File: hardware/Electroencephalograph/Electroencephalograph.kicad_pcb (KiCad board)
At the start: 2 copper layers, 162 parts, among them J1 Conn_01x08_Male, U1 ADS1298IPAG, U10 TC1017-xCT, U11 TPS60403, U2 OPA330xxD, U3 TMS320LF2406PZ, U4 REF5025, U5 OPA350, U6 ADUM2401BRWZ, U7 THI3-0511, U8 TC1017-xCT, U9 TC1017-xCT, X1 2M048

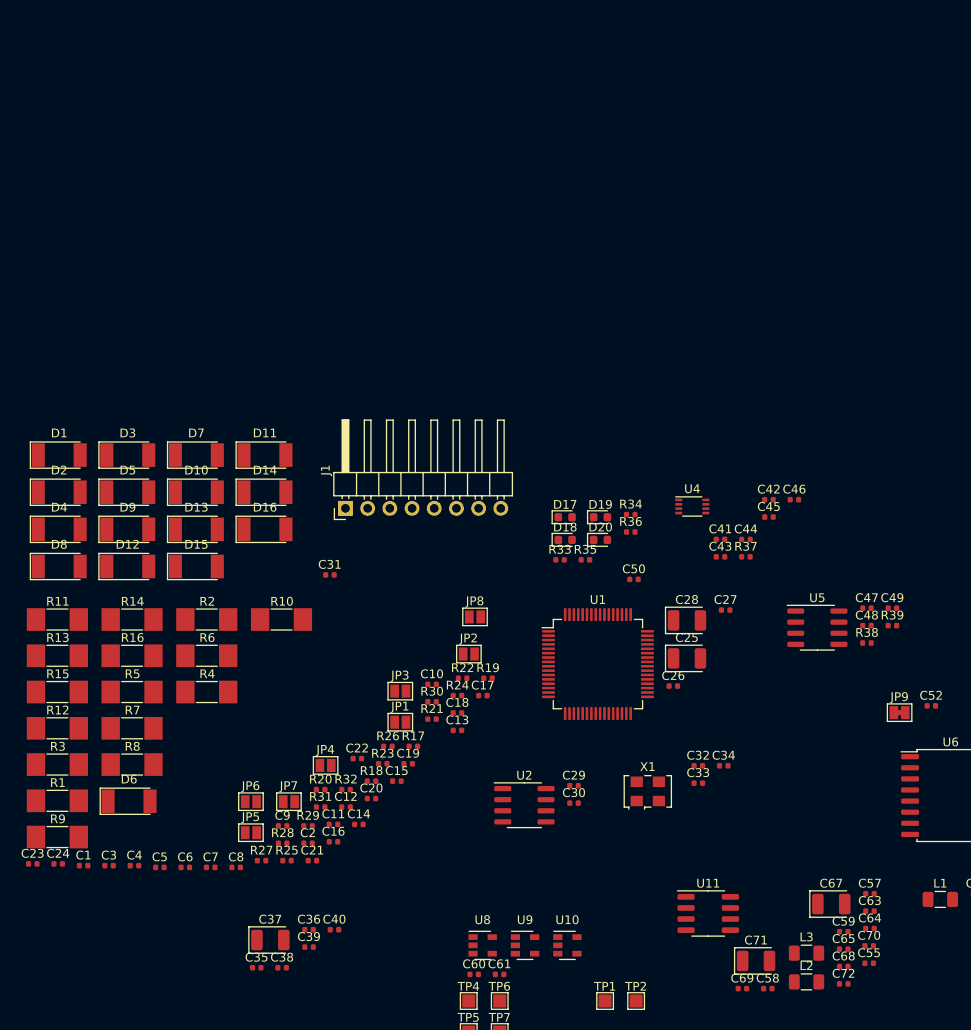
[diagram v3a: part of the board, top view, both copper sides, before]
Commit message: enqable separate electrodes for each point
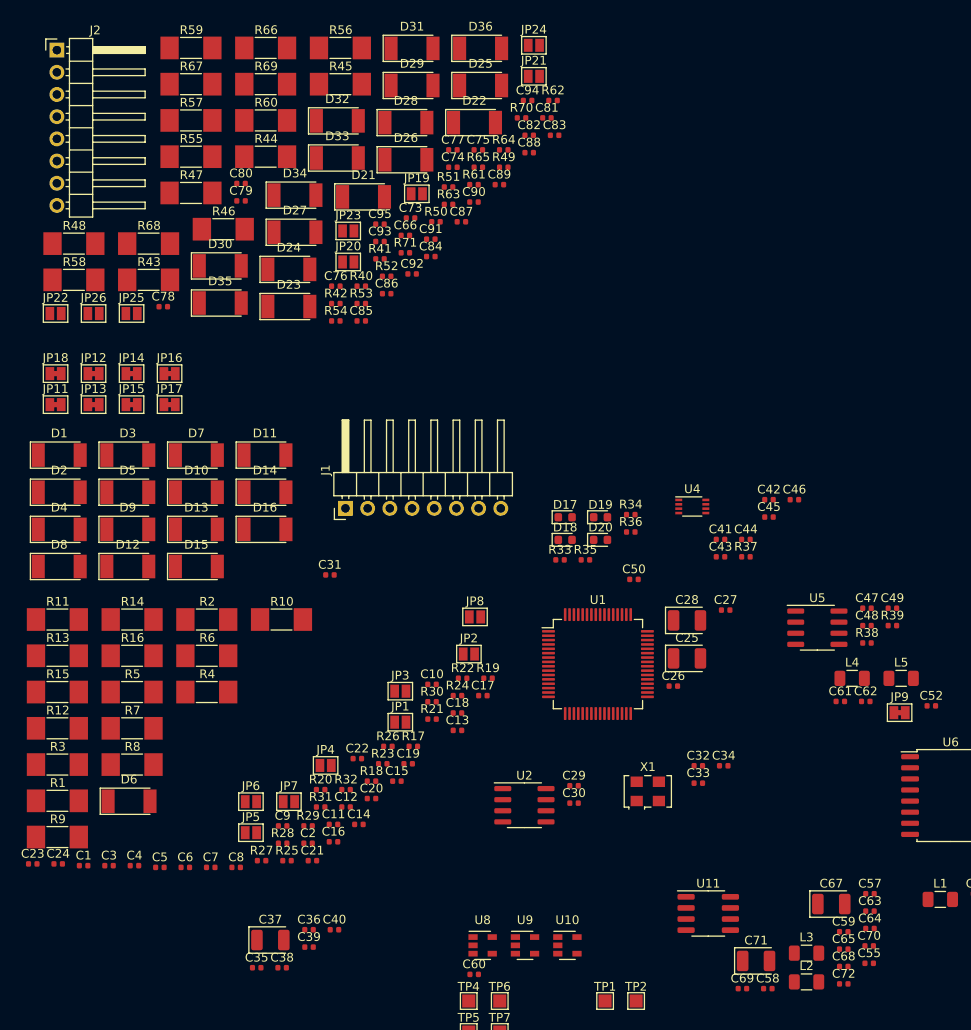
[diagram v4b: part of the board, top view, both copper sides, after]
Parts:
- added C62: 100n, Capacitor_SMD:C_0402_1005Metric, F.Cu at (225.2, 59.4)
- added C66: not mounted, Capacitor_SMD:C_0402_1005Metric, F.Cu at (172.5, 6.10)
- added C73: not mounted, Capacitor_SMD:C_0402_1005Metric, F.Cu at (173.1, 4.11)
- added C74: not mounted, Capacitor_SMD:C_0402_1005Metric, F.Cu at (177.9, -1.70)
- added C75: 47p, Capacitor_SMD:C_0402_1005Metric, F.Cu at (180.8, -3.69)
- added C76: 47p, Capacitor_SMD:C_0402_1005Metric, F.Cu at (164.5, 11.9)
- added C77: 47p, Capacitor_SMD:C_0402_1005Metric, F.Cu at (177.9, -3.69)
- added C78: 47p, Capacitor_SMD:C_0402_1005Metric, F.Cu at (144.8, 14.3)
- added C79: 47p, Capacitor_SMD:C_0402_1005Metric, F.Cu at (153.7, 2.15)
- added C80: 47p, Capacitor_SMD:C_0402_1005Metric, F.Cu at (153.7, 0.16)
- added C81: not mounted, Capacitor_SMD:C_0402_1005Metric, F.Cu at (188.7, -7.35)
- added C82: not mounted, Capacitor_SMD:C_0402_1005Metric, F.Cu at (186.6, -5.36)
- added C83: not mounted, Capacitor_SMD:C_0402_1005Metric, F.Cu at (189.5, -5.36)
- added C84: 47p, Capacitor_SMD:C_0402_1005Metric, F.Cu at (175.4, 8.52)
- added C85: 47p, Capacitor_SMD:C_0402_1005Metric, F.Cu at (167.4, 15.9)
- added C86: 47p, Capacitor_SMD:C_0402_1005Metric, F.Cu at (170.3, 12.8)
- added C87: 47p, Capacitor_SMD:C_0402_1005Metric, F.Cu at (178.9, 4.54)
- added C88: 47p, Capacitor_SMD:C_0402_1005Metric, F.Cu at (186.6, -3.37)
- added C89: 47p, Capacitor_SMD:C_0402_1005Metric, F.Cu at (183.2, 0.29)
- added C90: not mounted, Capacitor_SMD:C_0402_1005Metric, F.Cu at (180.3, 2.28)
- added C91: not mounted, Capacitor_SMD:C_0402_1005Metric, F.Cu at (175.4, 6.53)
- added C92: 47p, Capacitor_SMD:C_0402_1005Metric, F.Cu at (173.2, 10.5)
- added C93: 47p, Capacitor_SMD:C_0402_1005Metric, F.Cu at (169.6, 6.80)
- added C94: 47p, Capacitor_SMD:C_0402_1005Metric, F.Cu at (186.5, -9.34)
- added C95: 47p, Capacitor_SMD:C_0402_1005Metric, F.Cu at (169.6, 4.81)
- added D21: D, Diode_SMD:D_MELF, F.Cu at (167.7, 1.69)
- added D22: D, Diode_SMD:D_MELF, F.Cu at (180.4, -6.81)
- added D23: D, Diode_SMD:D_MELF, F.Cu at (159.1, 14.2)
- added D24: D, Diode_SMD:D_MELF, F.Cu at (159.1, 9.99)
- added D25: D, Diode_SMD:D_MELF, F.Cu at (181.1, -11.1)
- added D26: D, Diode_SMD:D_MELF, F.Cu at (172.5, -2.56)
- added D27: D, Diode_SMD:D_MELF, F.Cu at (159.8, 5.74)
- added D28: D, Diode_SMD:D_MELF, F.Cu at (172.5, -6.81)
- added D29: D, Diode_SMD:D_MELF, F.Cu at (173.2, -11.1)
- added D30: D, Diode_SMD:D_MELF, F.Cu at (151.3, 9.59)
- added D31: D, Diode_SMD:D_MELF, F.Cu at (173.2, -15.3)
- added D32: D, Diode_SMD:D_MELF, F.Cu at (164.7, -7.01)
- added D33: D, Diode_SMD:D_MELF, F.Cu at (164.7, -2.76)
- added D34: D, Diode_SMD:D_MELF, F.Cu at (159.8, 1.49)
- added D35: D, Diode_SMD:D_MELF, F.Cu at (151.3, 13.8)
- added D36: D, Diode_SMD:D_MELF, F.Cu at (181.1, -15.3)
- added J2: Conn_01x08_Male, Connector_PinHeader_2.54mm:PinHeader_1x08_P2.54mm_Horizontal, F.Cu at (132.6, -15.1)
- added JP11: NC, Jumper:SolderJumper-2_P1.3mm_Bridged_Pad1.0x1.5mm, F.Cu at (132.4, 25.5)
- added JP12: NC, Jumper:SolderJumper-2_P1.3mm_Bridged_Pad1.0x1.5mm, F.Cu at (136.8, 21.9)
- added JP13: NC, Jumper:SolderJumper-2_P1.3mm_Bridged_Pad1.0x1.5mm, F.Cu at (136.8, 25.5)
- added JP14: NC, Jumper:SolderJumper-2_P1.3mm_Bridged_Pad1.0x1.5mm, F.Cu at (141.1, 21.9)
- added JP15: NC, Jumper:SolderJumper-2_P1.3mm_Bridged_Pad1.0x1.5mm, F.Cu at (141.1, 25.5)
- added JP16: NC, Jumper:SolderJumper-2_P1.3mm_Bridged_Pad1.0x1.5mm, F.Cu at (145.5, 21.9)
- added JP17: NC, Jumper:SolderJumper-2_P1.3mm_Bridged_Pad1.0x1.5mm, F.Cu at (145.5, 25.5)
- added JP18: NC, Jumper:SolderJumper-2_P1.3mm_Bridged_Pad1.0x1.5mm, F.Cu at (132.4, 21.9)
- added JP19: Jumper_NO_Small, Jumper:SolderJumper-2_P1.3mm_Open_Pad1.0x1.5mm, F.Cu at (173.8, 1.34)
- added JP20: Jumper_NO_Small, Jumper:SolderJumper-2_P1.3mm_Open_Pad1.0x1.5mm, F.Cu at (165.9, 9.14)
- added JP21: Jumper_NO_Small, Jumper:SolderJumper-2_P1.3mm_Open_Pad1.0x1.5mm, F.Cu at (187.2, -12.1)
- added JP22: Jumper_NO_Small, Jumper:SolderJumper-2_P1.3mm_Open_Pad1.0x1.5mm, F.Cu at (132.4, 15.0)
- added JP23: Jumper_NO_Small, Jumper:SolderJumper-2_P1.3mm_Open_Pad1.0x1.5mm, F.Cu at (165.9, 5.59)
- added JP24: Jumper_NO_Small, Jumper:SolderJumper-2_P1.3mm_Open_Pad1.0x1.5mm, F.Cu at (187.2, -15.7)
- added JP25: Jumper_NO_Small, Jumper:SolderJumper-2_P1.3mm_Open_Pad1.0x1.5mm, F.Cu at (141.1, 15.0)
- added JP26: Jumper_NO_Small, Jumper:SolderJumper-2_P1.3mm_Open_Pad1.0x1.5mm, F.Cu at (136.8, 15.0)
- added L4: 3u3, Inductor_SMD:L_1206_3216Metric, F.Cu at (223.6, 56.8)
- added L5: 3u3, Inductor_SMD:L_1206_3216Metric, F.Cu at (229.2, 56.8)
- added R40: not mounted, Resistor_SMD:R_0402_1005Metric, F.Cu at (167.4, 11.9)
- added R41: not mounted, Resistor_SMD:R_0402_1005Metric, F.Cu at (169.6, 8.79)
- added R42: not mounted, Resistor_SMD:R_0402_1005Metric, F.Cu at (164.5, 13.9)
- added R43: 22k, Resistor_SMD:R_MELF_MMB-0207, F.Cu at (143.1, 11.2)
- added R44: 10k, Resistor_SMD:R_MELF_MMB-0207, F.Cu at (156.5, -2.91)
- added R45: 22k, Resistor_SMD:R_MELF_MMB-0207, F.Cu at (165.0, -11.2)
- added R46: 10k, Resistor_SMD:R_MELF_MMB-0207, F.Cu at (151.6, 5.39)
- added R47: 22k, Resistor_SMD:R_MELF_MMB-0207, F.Cu at (147.9, 1.24)
- added R48: 10k, Resistor_SMD:R_MELF_MMB-0207, F.Cu at (134.5, 7.04)
- added R49: not mounted, Resistor_SMD:R_0402_1005Metric, F.Cu at (183.7, -1.70)
- added R50: not mounted, Resistor_SMD:R_0402_1005Metric, F.Cu at (176.0, 4.54)
- added R51: not mounted, Resistor_SMD:R_0402_1005Metric, F.Cu at (177.4, 0.56)
- added R52: not mounted, Resistor_SMD:R_0402_1005Metric, F.Cu at (170.3, 10.8)
- added R53: not mounted, Resistor_SMD:R_0402_1005Metric, F.Cu at (167.4, 13.9)
- added R54: not mounted, Resistor_SMD:R_0402_1005Metric, F.Cu at (164.5, 15.9)
- added R55: 22k, Resistor_SMD:R_MELF_MMB-0207, F.Cu at (147.9, -2.91)
- added R56: 10k, Resistor_SMD:R_MELF_MMB-0207, F.Cu at (165.0, -15.4)
- added R57: 22k, Resistor_SMD:R_MELF_MMB-0207, F.Cu at (147.9, -7.06)
- added R58: 10k, Resistor_SMD:R_MELF_MMB-0207, F.Cu at (134.5, 11.2)
- added R59: 22k, Resistor_SMD:R_MELF_MMB-0207, F.Cu at (147.9, -15.4)
- added R60: 10k, Resistor_SMD:R_MELF_MMB-0207, F.Cu at (156.5, -7.06)
- added R61: not mounted, Resistor_SMD:R_0402_1005Metric, F.Cu at (180.3, 0.29)
- added R62: not mounted, Resistor_SMD:R_0402_1005Metric, F.Cu at (189.4, -9.34)
- added R63: not mounted, Resistor_SMD:R_0402_1005Metric, F.Cu at (177.4, 2.55)
- added R64: not mounted, Resistor_SMD:R_0402_1005Metric, F.Cu at (183.7, -3.69)
- added R65: not mounted, Resistor_SMD:R_0402_1005Metric, F.Cu at (180.8, -1.70)
- added R66: 22k, Resistor_SMD:R_MELF_MMB-0207, F.Cu at (156.5, -15.4)
- added R67: 10k, Resistor_SMD:R_MELF_MMB-0207, F.Cu at (147.9, -11.2)
- added R68: 22k, Resistor_SMD:R_MELF_MMB-0207, F.Cu at (143.1, 7.04)
- added R69: 10k, Resistor_SMD:R_MELF_MMB-0207, F.Cu at (156.5, -11.2)
- added R70: not mounted, Resistor_SMD:R_0402_1005Metric, F.Cu at (185.8, -7.35)
- added R71: not mounted, Resistor_SMD:R_0402_1005Metric, F.Cu at (172.5, 8.09)
- moved C61 50.0 mm to (222.2, 59.4)
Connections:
- net /EEGFrontend/ELECTRODE_1 renamed /EEGFrontendPositiveElectrode/ELECTRODE_1
- net /EEGFrontend/ELECTRODE_2 renamed /EEGFrontendPositiveElectrode/ELECTRODE_2
- net /EEGFrontend/ELECTRODE_3 renamed /EEGFrontendPositiveElectrode/ELECTRODE_3
- net /EEGFrontend/ELECTRODE_4 renamed /EEGFrontendPositiveElectrode/ELECTRODE_4
- net /EEGFrontend/ELECTRODE_5 renamed /EEGFrontendPositiveElectrode/ELECTRODE_5
- net /EEGFrontend/ELECTRODE_6 renamed /EEGFrontendPositiveElectrode/ELECTRODE_6
- net /EEGFrontend/ELECTRODE_7 renamed /EEGFrontendPositiveElectrode/ELECTRODE_7
- net /EEGFrontend/ELECTRODE_8 renamed /EEGFrontendPositiveElectrode/ELECTRODE_8
- net ECC_1 renamed ECC_1P
- net ECC_2 renamed ECC_2P
- net ECC_3 renamed ECC_3P
- net ECC_4 renamed ECC_4P
- net ECC_5 renamed ECC_5P
- net ECC_6 renamed ECC_6P
- net ECC_7 renamed ECC_7P
- net ECC_8 renamed ECC_8P
- C61 pad 1: VDDA -> Net-(C61-Pad1)
- C71 pad 1: Net-(C70-Pad1) -> Net-(C71-Pad1)
- C72 pad 1: Net-(C70-Pad1) -> Net-(C71-Pad1)
- TP6 pad 1: Net-(C70-Pad1) -> Net-(C71-Pad1)
- U1 pad 1: Net-(C31-Pad1) -> ECC_8N
- U1 pad 11: Net-(C31-Pad1) -> ECC_3N
- U1 pad 13: Net-(C31-Pad1) -> ECC_2N
- U1 pad 15: Net-(C31-Pad1) -> ECC_1N
- U1 pad 3: Net-(C31-Pad1) -> ECC_7N
- U1 pad 5: Net-(C31-Pad1) -> ECC_6N
- U1 pad 7: Net-(C31-Pad1) -> ECC_5N
- U1 pad 9: Net-(C31-Pad1) -> ECC_4N
- U10 pad 1: Net-(C70-Pad1) -> Net-(C71-Pad1)
- U10 pad 3: Net-(C70-Pad1) -> Net-(C71-Pad1)
- U8 pad 5: VDDA -> Net-(C61-Pad1)

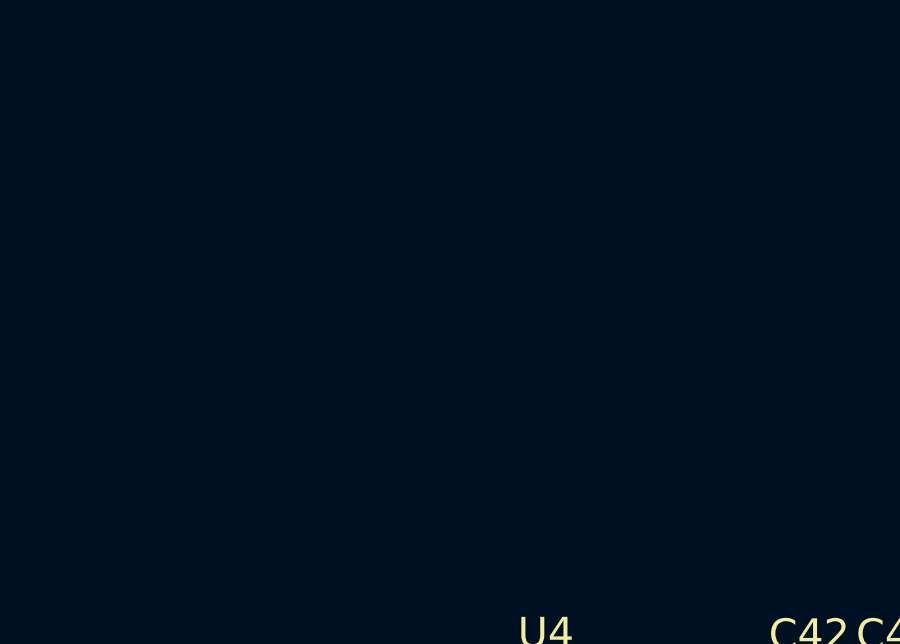
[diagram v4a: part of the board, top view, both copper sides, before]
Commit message: removed external clk and vref
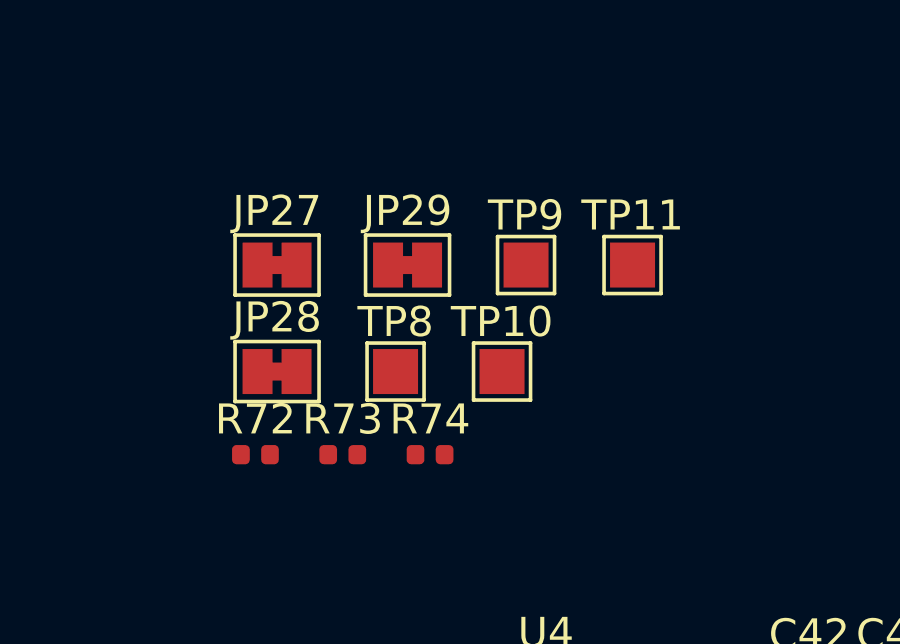
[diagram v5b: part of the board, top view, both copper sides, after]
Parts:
- added JP27: NC, Jumper:SolderJumper-2_P1.3mm_Bridged_Pad1.0x1.5mm, F.Cu at (196.3, 22.9)
- added JP28: NC, Jumper:SolderJumper-2_P1.3mm_Bridged_Pad1.0x1.5mm, F.Cu at (196.3, 26.4)
- added JP29: NC, Jumper:SolderJumper-2_P1.3mm_Bridged_Pad1.0x1.5mm, F.Cu at (200.7, 22.9)
- added R72: NC, Resistor_SMD:R_0402_1005Metric, F.Cu at (195.6, 29.2)
- added R73: NC, Resistor_SMD:R_0402_1005Metric, F.Cu at (198.5, 29.2)
- added R74: NC, Resistor_SMD:R_0402_1005Metric, F.Cu at (201.4, 29.2)
- added TP10: TestPoint, TestPoint:TestPoint_Pad_1.5x1.5mm, F.Cu at (203.8, 26.4)
- added TP11: TestPoint, TestPoint:TestPoint_Pad_1.5x1.5mm, F.Cu at (208.2, 22.9)
- added TP8: TestPoint, TestPoint:TestPoint_Pad_1.5x1.5mm, F.Cu at (200.3, 26.4)
- added TP9: TestPoint, TestPoint:TestPoint_Pad_1.5x1.5mm, F.Cu at (204.6, 22.9)
- C1, C2, C21, C22, C23, C24, C3, C4, C66, C73, C74, C81, C82, C83, C90, C91, R17, R18, R19, R20, R21, R22, R23, R24, R25, R26, R27, R28, R29, R30, R31, R32, R40, R41, R42, R49, R50, R51, R52, R53, R54, R61, R62, R63, R64, R65, R70, R71: value not mounted -> NC
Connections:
- U1 pad 32: (no net) -> VDDA
- U1 pad 34: (no net) -> EEG_MOSI
- U1 pad 35: (no net) -> Net-(JP28-Pad2)
- U1 pad 36: (no net) -> Net-(JP27-Pad2)
- U1 pad 38: (no net) -> Net-(JP29-Pad2)
- U1 pad 39: (no net) -> EEG_CS
- U1 pad 40: (no net) -> EEG_SCK
- U1 pad 43: (no net) -> EEG_MISO
- U6 pad 11: (no net) -> EEG_MISO
- U6 pad 12: (no net) -> EEG_CS
- U6 pad 13: (no net) -> EEG_MOSI
- U6 pad 14: (no net) -> EEG_SCK

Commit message: draft of PCB routing
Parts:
- removed C94, C95: 47p, Capacitor_SMD:C_0402_1005Metric
- removed R72, R73, R74: NC, Resistor_SMD:R_0402_1005Metric
- removed U10, U8, U9: TC1017-xCT, Package_TO_SOT_SMD:SOT-23-5
- removed U11: TPS60403, Package_SO:SOP-8_3.76x4.96mm_P1.27mm
- removed U7: THI3-0511, Relay_THT:Relay_DPDT_Omron_G6K-2P-Y
- removed X1: 2M048, Oscillator:Oscillator_SMD_EuroQuartz_XO53-4Pin_5.0x3.2mm
- added JP30: Jumper_NO_Small, Jumper:SolderJumper-2_P1.3mm_Open_Pad1.0x1.5mm, F.Cu at (79.4, 21.8)
- added JP31: Jumper_NO_Small, Jumper:SolderJumper-2_P1.3mm_Open_Pad1.0x1.5mm, F.Cu at (79.4, 37.1)
- added JP32: Jumper_NO_Small, Jumper:SolderJumper-2_P1.3mm_Open_Pad1.0x1.5mm, F.Cu at (79.4, 27.9)
- added L6: 22u, Inductor_SMD:L_7.3x7.3_H3.5, F.Cu at (120.9, 57.3)
- added TP12: TestPoint, TestPoint:TestPoint_Pad_1.5x1.5mm, F.Cu at (136.0, 55.3)
- added TP13: TestPoint, TestPoint:TestPoint_Pad_1.5x1.5mm, F.Cu at (137.9, 50.8)
- C1, C2, C21, C22, C3, C4, C73, C74, C81, C82, C83, C90, C91: value NC -> 47p
- C16, C17, C18, C7, C76, C77, C78, C8, C85, C86, C87, C9, C92, C93: value 47p -> NC
- C25: value 22u -> 1n; footprint Capacitor_Tantalum_SMD:CP_EIA-3528-21_Kemet-B -> Capacitor_SMD:C_0402_1005Metric
- C27, C35, C62: value 100n -> 2u2
- C28: footprint Capacitor_Tantalum_SMD:CP_EIA-3528-21_Kemet-B -> Capacitor_SMD:C_0402_1005Metric
- C29, C36, C56, C58, C59: value 100n -> 1u
- C31: value 1n -> 100n
- C32, C34, C40, C41, C69: value 1u -> 100n
- C38: value 100n -> 22u; footprint Capacitor_SMD:C_0402_1005Metric -> Capacitor_Tantalum_SMD:CP_EIA-3528-21_Kemet-B
- C45: value 10u -> 1u
- C46: value 100u -> 1u
- C48: value 22n -> 100n
- C49, C52: value 100n -> 220u; footprint Capacitor_SMD:C_0402_1005Metric -> Capacitor_SMD:CP_Elec_6.3x5.8
- C57: value 1u -> 100u; footprint Capacitor_SMD:C_0402_1005Metric -> Capacitor_SMD:CP_Elec_6.3x5.8
- C60: value 1u -> 100u; footprint Capacitor_SMD:C_0402_1005Metric -> Capacitor_Tantalum_SMD:CP_EIA-3528-21_Kemet-B
- C61, C63, C64, C65: value 1u -> 2u2
- C66: value NC -> 2u2
- C67: value 22u -> 100n; footprint Capacitor_Tantalum_SMD:CP_EIA-3528-21_Kemet-B -> Capacitor_SMD:C_0402_1005Metric
- C70, C72: value 1u -> 47p
- C71: value 22u -> 47p; footprint Capacitor_Tantalum_SMD:CP_EIA-3528-21_Kemet-B -> Capacitor_SMD:C_0402_1005Metric
- D1, D10, D11, D12, D13, D14, D15, D16, D2, D21, D22, D23, D24, D25, D26, D27, D28, D29, D3, D30, D31, D32, D33, D34, D35, D36, D4, D5, D6, D7, D8, D9, JP11, JP12, JP13, JP14, JP15, JP16: moved to B.Cu
- JP10, JP9: value Jumper_NC_Small -> NC; moved to B.Cu
- JP19, JP20, JP21, JP22: value Jumper_NO_Small -> NC; footprint Jumper:SolderJumper-2_P1.3mm_Open_Pad1.0x1.5mm -> Jumper:SolderJumper-2_P1.3mm_Bridged_Pad1.0x1.5mm
- JP23, JP24: value Jumper_NO_Small -> Jumper_NC_Small; footprint Jumper:SolderJumper-2_P1.3mm_Open_Pad1.0x1.5mm -> Jumper:SolderJumper-2_P1.3mm_Bridged_Pad1.0x1.5mm
- JP27, JP28, JP29: value NC -> Jumper_NO_Small; footprint Jumper:SolderJumper-2_P1.3mm_Bridged_Pad1.0x1.5mm -> Jumper:SolderJumper-2_P1.3mm_Open_Pad1.0x1.5mm
- L1, L2, L3, L4, L5: value 3u3 -> 22u; footprint Inductor_SMD:L_1206_3216Metric -> Inductor_SMD:L_7.3x7.3_H3.5
- R10, R12, R46, R48, R58, R60, R69, R8: value 10k -> NC; footprint Resistor_SMD:R_MELF_MMB-0207 -> Resistor_SMD:R_0402_1005Metric
- R11, R47, R59, R68, R7, R9: value 22k -> NC; footprint Resistor_SMD:R_MELF_MMB-0207 -> Resistor_SMD:R_0402_1005Metric
- R14, R2: value 10k -> 22k
- R17, R18, R27, R28: value NC -> 10k; footprint Resistor_SMD:R_0402_1005Metric -> Resistor_SMD:R_MELF_MMB-0207
- R25, R26, R40, R41, R42, R52, R53, R54, R64, R65: value NC -> 22k; footprint Resistor_SMD:R_0402_1005Metric -> Resistor_SMD:R_MELF_MMB-0207
- R37: value 100R -> NC
- R38: value 10R -> NC
- R39: value 100k -> NC
- R43, R45, R5, R55, R57, R66: value 22k -> 10k
- U4: value REF5025 -> THI3-0511; footprint Package_SO:VSSOP-8_2.3x2mm_P0.5mm -> Relay_THT:Relay_DPDT_Omron_G6K-2P-Y
- U5: value OPA350 -> ADUM2401BRWZ; footprint Package_SO:SOIC-8_3.9x4.9mm_P1.27mm -> Package_SO:SOIC-16W_7.5x10.3mm_P1.27mm
- U6: value ADUM2401BRWZ -> TPS60403; footprint Package_SO:SOIC-16W_7.5x10.3mm_P1.27mm -> Package_SO:SOP-8_3.76x4.96mm_P1.27mm
- moved U3 186.8 mm to (88.9, 93.5)
- moved C72 169.2 mm to (67.1, 25.4), turned to 90 degrees
- moved C70 166.9 mm to (67.1, 35.0), turned to 90 degrees
- moved JP10 159.0 mm to (84.8, 58.9), turned to 180 degrees
- moved C71 152.5 mm to (67.1, 43.7), turned to 90 degrees
- moved JP9 144.3 mm to (84.8, 65.0), turned to 180 degrees
- moved C47 137.2 mm to (89.4, 29.5)
- moved L1 137.1 mm to (106.7, 30.5), turned to 90 degrees
- moved L2 134.0 mm to (99.1, 30.5), turned to 90 degrees
- moved C48 133.1 mm to (94.0, 29.5)
- moved C81 127.7 mm to (67.1, 31.5), turned to 90 degrees
- moved R64 125.8 mm to (62.1, 28.4), turned to 180 degrees
- moved R65 125.1 mm to (62.1, 37.6), turned to 180 degrees
- moved C88 123.8 mm to (67.0, 28.4), turned to 90 degrees
- moved R39 122.6 mm to (105.6, 48.8), turned to 180 degrees
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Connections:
- C1 pad 1: ECC_1P -> Net-(C1-Pad1)
- C1 pad 2: Net-(C1-Pad2) -> GNDA
- C16 pad 1: Net-(C16-Pad1) -> ECC_1N
- C16 pad 2: GNDA -> Net-(C13-Pad1)
- C17 pad 1: Net-(C17-Pad1) -> ECC_3P
- C17 pad 2: GNDA -> Net-(C15-Pad1)
- C18 pad 1: Net-(C18-Pad1) -> ECC_4N
- C18 pad 2: GNDA -> Net-(C14-Pad1)
- C2 pad 1: ECC_2P -> Net-(C2-Pad1)
- C2 pad 2: Net-(C2-Pad2) -> GNDA
- C21 pad 1: ECC_6P -> Net-(C21-Pad1)
- C21 pad 2: Net-(C16-Pad1) -> GNDA
- C22 pad 1: ECC_5P -> Net-(C22-Pad1)
- C22 pad 2: Net-(C14-Pad1) -> GNDA
- C23 pad 1: ECC_8P -> ECC_2P
- C23 pad 2: Net-(C20-Pad1) -> Net-(C22-Pad1)
- C24 pad 1: ECC_7P -> ECC_3N
- C24 pad 2: Net-(C18-Pad1) -> Net-(C21-Pad1)
- C26 pad 1: Net-(C26-Pad1) -> VDDA
- C26 pad 2: VDDA -> GNDA
- C28 pad 1: VDDA -> Net-(C28-Pad1)
- C29 pad 1: VDDA -> GNDA
- C29 pad 2: GNDA -> VDDA
- C3 pad 1: ECC_4P -> Net-(C3-Pad1)
- C3 pad 2: Net-(C12-Pad1) -> GNDA
- C30 pad 1: VDDA -> GNDA
- C30 pad 2: GNDA -> VDDA
- C31 pad 1: Net-(C31-Pad1) -> Net-(C28-Pad1)
- C31 pad 2: VDDA -> GNDA
- C32 pad 1: Net-(C26-Pad1) -> GNDA
- C33 pad 1: Net-(C33-Pad1) -> GNDA
- C34 pad 1: Net-(C34-Pad1) -> VDDA
- C34 pad 2: VDDA -> GNDA
- C35 pad 2: VDDA -> GNDA
- C36 pad 1: VDDA -> Net-(C36-Pad1)
- C36 pad 2: VDDA -> GNDA
- C37 pad 1: /EEGAcquisition/V_REF -> Net-(C37-Pad1)
- C37 pad 2: VDDA -> GNDA
- C38 pad 1: /EEGAcquisition/V_REF -> Net-(C38-Pad1)
- C38 pad 2: VDDA -> GNDA
- C39 pad 1: VDDA -> Net-(C39-Pad1)
- C39 pad 2: VDDA -> GNDA
- C4 pad 1: ECC_3P -> Net-(C4-Pad1)
- C4 pad 2: Net-(C10-Pad1) -> GNDA
- C40 pad 1: VDDA -> Net-(C37-Pad1)
- C40 pad 2: VDDA -> GNDA
- C41 pad 1: VDDA -> GNDA
- C41 pad 2: VDDA -> Net-(C41-Pad2)
- C42 pad 1: VDDA -> Net-(C42-Pad1)
- C42 pad 2: VDDA -> GNDA
- C43 pad 2: VDDA -> GNDA
- C44 pad 1: Net-(C44-Pad1) -> GNDA
- C45 pad 1: Net-(C45-Pad1) -> VDDA
- C45 pad 2: VDDA -> GNDA
- C46 pad 1: Net-(C46-Pad1) -> VDDA
- C46 pad 2: VDDA -> GNDA
- C47 pad 1: GNDA -> VDDA
- C47 pad 2: VDDA -> GNDA
- C48 pad 1: Net-(C48-Pad1) -> VDDA
- C48 pad 2: Net-(C48-Pad2) -> GNDA
- C49 pad 1: GNDA -> VDDA
- C49 pad 2: VDDA -> GNDA
- C50 pad 1: VDDA -> Net-(C50-Pad1)
- C52 pad 1: VDDA -> Net-(C52-Pad1)
- C53 pad 1: ECC_POWER_SUPPLY -> Net-(C52-Pad1)
- C55 pad 1: VDDA -> ECC_POWER_SUPPLY
- C56 pad 1: Net-(C56-Pad1) -> ECC_POWER_SUPPLY
- C57 pad 1: VDDA -> Net-(C57-Pad1)
- C57 pad 2: VDDA -> GNDA
- C58 pad 1: VDDA -> (no net)
- C58 pad 2: VDDA -> Net-(C58-Pad2)
- C59 pad 1: VDDA -> Net-(C59-Pad1)
- C6 pad 1: Net-(C1-Pad2) -> Net-(C6-Pad1)
- C60 pad 1: ECC_POWER_SUPPLY -> Net-(C60-Pad1)
- C61 pad 1: Net-(C61-Pad1) -> ECC_POWER_SUPPLY
- C62 pad 1: VDDA -> ECC_POWER_SUPPLY
- C63 pad 1: Net-(C63-Pad1) -> Net-(C60-Pad1)
- C64 pad 1: ECC_POWER_SUPPLY -> VDDA
- C65 pad 1: (no net) -> VDDA
- C65 pad 2: Net-(C65-Pad2) -> GNDA
- C66 pad 1: ECC_1N -> VDDA
- C66 pad 2: Net-(C66-Pad2) -> GNDA
- C67 pad 1: ECC_POWER_SUPPLY -> VDDA
- C68 pad 1: ECC_POWER_SUPPLY -> VDDA
- C68 pad 2: GNDA -> VDDA
- C69 pad 1: Net-(C69-Pad1) -> VDDA
- C69 pad 2: GNDA -> VDDA
- C7 pad 1: Net-(C7-Pad1) -> ECC_1P
- C7 pad 2: GNDA -> Net-(C5-Pad1)
- C72 pad 1: Net-(C71-Pad1) -> Net-(C72-Pad1)
- C73 pad 1: ECC_2N -> Net-(C73-Pad1)
- C73 pad 2: Net-(C73-Pad2) -> GNDA
- C74 pad 1: ECC_3N -> Net-(C74-Pad1)
- C74 pad 2: Net-(C74-Pad2) -> GNDA
- C76 pad 1: Net-(C66-Pad2) -> ECC_5P
- C76 pad 2: GNDA -> Net-(C74-Pad1)
- C77 pad 1: Net-(C77-Pad1) -> ECC_6N
- C77 pad 2: GNDA -> Net-(C73-Pad1)
- C78 pad 1: Net-(C73-Pad2) -> ECC_8P
- C78 pad 2: GNDA -> Net-(C75-Pad1)
- C8 pad 1: Net-(C2-Pad2) -> ECC_2N
- C8 pad 2: GNDA -> Net-(C4-Pad1)
- C80 pad 1: Net-(C74-Pad2) -> Net-(C80-Pad1)
- C81 pad 1: ECC_6N -> Net-(C81-Pad1)
- C81 pad 2: Net-(C81-Pad2) -> GNDA
- C82 pad 1: ECC_4N -> Net-(C82-Pad1)
- C82 pad 2: Net-(C82-Pad2) -> GNDA
- C83 pad 1: ECC_5N -> Net-(C83-Pad1)
- C83 pad 2: Net-(C83-Pad2) -> GNDA
- C85 pad 1: Net-(C81-Pad2) -> ECC_5N
- C85 pad 2: GNDA -> Net-(C82-Pad1)
- C86 pad 1: Net-(C86-Pad1) -> ECC_7P
- C86 pad 2: GNDA -> Net-(C84-Pad1)
- C87 pad 1: Net-(C82-Pad2) -> ECC_8N
- C87 pad 2: GNDA -> Net-(C83-Pad1)
- C89 pad 1: Net-(C83-Pad2) -> Net-(C89-Pad1)
- C9 pad 1: Net-(C9-Pad1) -> ECC_4P
- C9 pad 2: GNDA -> Net-(C6-Pad1)
- C90 pad 1: ECC_8N -> Net-(C90-Pad1)
- C90 pad 2: Net-(C90-Pad2) -> GNDA
- C91 pad 1: ECC_7N -> Net-(C91-Pad1)
- C91 pad 2: Net-(C91-Pad2) -> GNDA
- C92 pad 1: Net-(C92-Pad1) -> ECC_6P
- C92 pad 2: GNDA -> Net-(C91-Pad1)
- C93 pad 1: Net-(C90-Pad2) -> ECC_7N
- C93 pad 2: GNDA -> Net-(C90-Pad1)
- D1 pad 2: Net-(C1-Pad2) -> Net-(C5-Pad1)
- D10 pad 1: VDDA -> Net-(C15-Pad1)
- D10 pad 2: Net-(C14-Pad1) -> VDDA
- D11 pad 1: Net-(C16-Pad1) -> VDDA
- D11 pad 2: VDDA -> Net-(C14-Pad1)
- D13 pad 2: Net-(C20-Pad1) -> Net-(C22-Pad1)
- D14 pad 1: VDDA -> Net-(C22-Pad1)
- D14 pad 2: Net-(D14-Pad2) -> VDDA
- D15 pad 1: Net-(C20-Pad1) -> VDDA
- D15 pad 2: VDDA -> Net-(C21-Pad1)
- D16 pad 1: Net-(D14-Pad2) -> Net-(C21-Pad1)
- D2 pad 1: VDDA -> Net-(C5-Pad1)
- D2 pad 2: Net-(C2-Pad2) -> VDDA
- D21 pad 2: Net-(C66-Pad2) -> Net-(C74-Pad1)
- D22 pad 1: VDDA -> Net-(C74-Pad1)
- D22 pad 2: Net-(C73-Pad2) -> VDDA
- D23 pad 2: Net-(C74-Pad2) -> Net-(C73-Pad1)
- D24 pad 1: Net-(C74-Pad2) -> Net-(C73-Pad1)
- D25 pad 1: Net-(C66-Pad2) -> VDDA
- D25 pad 2: VDDA -> Net-(C75-Pad1)
- D26 pad 1: Net-(C73-Pad2) -> Net-(C75-Pad1)
- D27 pad 2: Net-(C81-Pad2) -> Net-(C82-Pad1)
- D28 pad 1: VDDA -> Net-(C82-Pad1)
- D28 pad 2: Net-(C82-Pad2) -> VDDA
- D29 pad 2: Net-(C83-Pad2) -> Net-(C84-Pad1)
- D3 pad 1: Net-(C1-Pad2) -> VDDA
- D3 pad 2: VDDA -> Net-(C4-Pad1)
- D30 pad 1: Net-(C81-Pad2) -> Net-(C84-Pad1)
- D31 pad 1: Net-(C82-Pad2) -> VDDA
- D31 pad 2: VDDA -> Net-(C83-Pad1)
- D32 pad 1: Net-(C83-Pad2) -> Net-(C83-Pad1)
- D33 pad 2: Net-(C90-Pad2) -> Net-(C91-Pad1)
- D34 pad 1: VDDA -> Net-(C91-Pad1)
- D34 pad 2: Net-(D34-Pad2) -> VDDA
- D35 pad 1: Net-(C90-Pad2) -> VDDA
- D35 pad 2: VDDA -> Net-(C90-Pad1)
- D36 pad 1: Net-(D34-Pad2) -> Net-(C90-Pad1)
- D4 pad 1: Net-(C2-Pad2) -> Net-(C4-Pad1)
- D5 pad 2: Net-(C12-Pad1) -> Net-(C6-Pad1)
- D6 pad 1: VDDA -> Net-(C6-Pad1)
- D6 pad 2: Net-(C10-Pad1) -> VDDA
- D7 pad 1: Net-(C10-Pad1) -> VDDA
- D7 pad 2: VDDA -> Net-(C13-Pad1)
- D8 pad 1: Net-(C12-Pad1) -> Net-(C13-Pad1)
- D9 pad 2: Net-(C16-Pad1) -> Net-(C15-Pad1)
- J1 pad 1: /EEGFrontendPositiveElectrode/ELECTRODE_1 -> /EEGFrontendElectrode1To4/ELECTRODE_1
- J1 pad 2: /EEGFrontendPositiveElectrode/ELECTRODE_2 -> /EEGFrontendElectrode1To4/ELECTRODE_2
- J1 pad 3: /EEGFrontendPositiveElectrode/ELECTRODE_3 -> /EEGFrontendElectrode1To4/ELECTRODE_3
- J1 pad 4: /EEGFrontendPositiveElectrode/ELECTRODE_4 -> /EEGFrontendElectrode1To4/ELECTRODE_4
- J1 pad 5: /EEGFrontendPositiveElectrode/ELECTRODE_5 -> /EEGFrontendElectrode1To4/ELECTRODE_5
- J1 pad 6: /EEGFrontendPositiveElectrode/ELECTRODE_6 -> /EEGFrontendElectrode1To4/ELECTRODE_6
- J1 pad 7: /EEGFrontendPositiveElectrode/ELECTRODE_7 -> /EEGFrontendElectrode1To4/ELECTRODE_7
- J1 pad 8: /EEGFrontendPositiveElectrode/ELECTRODE_8 -> /EEGFrontendElectrode1To4/ELECTRODE_8
- J2 pad 1: /EEGFrontendNegativeElectrode/ELECTRODE_1 -> /EEGFrontendElectrode5To8/ELECTRODE_1
- J2 pad 2: /EEGFrontendNegativeElectrode/ELECTRODE_2 -> /EEGFrontendElectrode5To8/ELECTRODE_2
- J2 pad 3: /EEGFrontendNegativeElectrode/ELECTRODE_3 -> /EEGFrontendElectrode5To8/ELECTRODE_3
- J2 pad 4: /EEGFrontendNegativeElectrode/ELECTRODE_4 -> /EEGFrontendElectrode5To8/ELECTRODE_4
- J2 pad 5: /EEGFrontendNegativeElectrode/ELECTRODE_5 -> /EEGFrontendElectrode5To8/ELECTRODE_5
- J2 pad 6: /EEGFrontendNegativeElectrode/ELECTRODE_6 -> /EEGFrontendElectrode5To8/ELECTRODE_6
- J2 pad 7: /EEGFrontendNegativeElectrode/ELECTRODE_7 -> /EEGFrontendElectrode5To8/ELECTRODE_7
- J2 pad 8: /EEGFrontendNegativeElectrode/ELECTRODE_8 -> /EEGFrontendElectrode5To8/ELECTRODE_8
- JP1 pad 1: Net-(C1-Pad2) -> Net-(C5-Pad1)
- JP10 pad 1: Net-(JP10-Pad1) -> Net-(C25-Pad1)
- JP10 pad 2: VDDA -> ECC_2N
- JP11 pad 1: Net-(C31-Pad1) -> Net-(C25-Pad1)
- JP11 pad 2: ECC_1N -> ECC_3N
- JP12 pad 1: Net-(C31-Pad1) -> Net-(C25-Pad1)
- JP12 pad 2: ECC_2N -> ECC_4N
- JP13 pad 1: Net-(C31-Pad1) -> Net-(C25-Pad1)
- JP13 pad 2: ECC_3N -> ECC_5N
- JP14 pad 1: Net-(C31-Pad1) -> Net-(C25-Pad1)
- JP14 pad 2: ECC_4N -> ECC_6N
- JP15 pad 1: Net-(C31-Pad1) -> Net-(C25-Pad1)
- JP15 pad 2: ECC_5N -> ECC_7N
- JP16 pad 1: Net-(C31-Pad1) -> Net-(C25-Pad1)
- JP16 pad 2: ECC_6N -> ECC_8N
- JP17 pad 1: Net-(C31-Pad1) -> VDDA
- JP17 pad 2: ECC_7N -> Net-(JP17-Pad2)
- JP18 pad 1: Net-(C31-Pad1) -> (no net)
- JP18 pad 2: ECC_8N -> Net-(JP18-Pad2)
- JP19 pad 1: Net-(C66-Pad2) -> GNDA
- JP19 pad 2: ECC_1N -> Net-(JP19-Pad2)
- JP2 pad 1: Net-(C2-Pad2) -> Net-(C4-Pad1)
- JP2 pad 2: ECC_2P -> ECC_2N
- JP20 pad 1: Net-(C73-Pad2) -> VDDA
- JP20 pad 2: ECC_2N -> Net-(JP20-Pad2)
- JP21 pad 1: Net-(C74-Pad2) -> VDDA
- JP21 pad 2: ECC_3N -> Net-(JP21-Pad2)
- JP22 pad 1: Net-(C81-Pad2) -> VDDA
- JP22 pad 2: ECC_6N -> Net-(JP22-Pad2)
- JP23 pad 1: Net-(C82-Pad2) -> Net-(JP23-Pad1)
- JP23 pad 2: ECC_4N -> VDDA
- JP24 pad 1: Net-(C83-Pad2) -> Net-(JP24-Pad1)
- JP24 pad 2: ECC_5N -> VDDA
- JP25 pad 1: Net-(C90-Pad2) -> Net-(C74-Pad1)
- JP25 pad 2: ECC_8N -> ECC_5P
- JP26 pad 1: Net-(C91-Pad2) -> Net-(C73-Pad1)
- JP26 pad 2: ECC_7N -> ECC_6N
- JP27 pad 1: VDDA -> Net-(C75-Pad1)
- JP27 pad 2: Net-(JP27-Pad2) -> ECC_8P
- JP28 pad 1: VDDA -> Net-(C82-Pad1)
- JP28 pad 2: Net-(JP28-Pad2) -> ECC_5N
- JP29 pad 1: VDDA -> Net-(C84-Pad1)
- JP29 pad 2: Net-(JP29-Pad2) -> ECC_7P
- JP3 pad 1: Net-(C12-Pad1) -> Net-(C6-Pad1)
- JP4 pad 1: Net-(C10-Pad1) -> Net-(C13-Pad1)
- JP4 pad 2: ECC_3P -> ECC_1N
- JP5 pad 1: Net-(C16-Pad1) -> Net-(C15-Pad1)
- JP5 pad 2: ECC_6P -> ECC_3P
- JP6 pad 2: ECC_5P -> ECC_4N
- JP7 pad 1: Net-(C20-Pad1) -> Net-(C22-Pad1)
- JP7 pad 2: ECC_8P -> ECC_2P
- JP8 pad 1: Net-(C18-Pad1) -> Net-(C21-Pad1)
- JP8 pad 2: ECC_7P -> ECC_3N
- JP9 pad 1: Net-(JP9-Pad1) -> Net-(C25-Pad1)
- JP9 pad 2: VDDA -> ECC_1N
- L1 pad 1: Net-(C56-Pad1) -> Net-(C41-Pad2)
- L1 pad 2: ECC_POWER_SUPPLY -> VDDA
- L2 pad 1: Net-(C63-Pad1) -> Net-(C42-Pad1)
- L3 pad 1: Net-(C69-Pad1) -> VDDA
- L3 pad 2: VDDA -> Net-(C50-Pad1)
- L4 pad 1: Net-(C61-Pad1) -> Net-(C52-Pad1)
- L4 pad 2: VDDA -> ECC_POWER_SUPPLY
- L5 pad 1: Net-(C71-Pad1) -> Net-(C57-Pad1)
- L5 pad 2: Net-(C70-Pad1) -> ECC_POWER_SUPPLY
- R1 pad 1: Net-(C5-Pad1) -> Net-(C1-Pad1)
- R1 pad 2: /EEGFrontendPositiveElectrode/ELECTRODE_1 -> /EEGFrontendElectrode1To4/ELECTRODE_4
- R10 pad 1: Net-(C14-Pad1) -> VDDA
- R10 pad 2: Net-(C13-Pad1) -> ECC_2N
- R11 pad 1: Net-(C15-Pad1) -> ECC_4P
- R11 pad 2: /EEGFrontendPositiveElectrode/ELECTRODE_6 -> VDDA
- R12 pad 1: Net-(C16-Pad1) -> VDDA
- R12 pad 2: Net-(C15-Pad1) -> ECC_4P
- R13 pad 1: Net-(C17-Pad1) -> Net-(C10-Pad1)
- R13 pad 2: /EEGFrontendPositiveElectrode/ELECTRODE_7 -> /EEGFrontendElectrode1To4/ELECTRODE_2
- R14 pad 1: Net-(C18-Pad1) -> Net-(C11-Pad1)
- R14 pad 2: Net-(C17-Pad1) -> /EEGFrontendElectrode1To4/ELECTRODE_8
- R15 pad 1: Net-(C19-Pad1) -> Net-(C12-Pad1)
- R15 pad 2: /EEGFrontendPositiveElectrode/ELECTRODE_8 -> /EEGFrontendElectrode1To4/ELECTRODE_5
- R16 pad 1: Net-(C20-Pad1) -> Net-(C13-Pad1)
- R16 pad 2: Net-(C19-Pad1) -> Net-(C10-Pad1)
- R17 pad 1: ECC_1P -> Net-(C14-Pad1)
- R17 pad 2: VDDA -> Net-(C11-Pad1)
- R18 pad 1: ECC_2P -> Net-(C15-Pad1)
- R18 pad 2: VDDA -> Net-(C12-Pad1)
- R19 pad 1: VDDA -> ECC_1N
- R19 pad 2: ECC_1P -> VDDA
- R2 pad 1: Net-(C1-Pad2) -> Net-(C2-Pad1)
- R2 pad 2: Net-(C5-Pad1) -> /EEGFrontendElectrode1To4/ELECTRODE_1
- R20 pad 2: ECC_2P -> ECC_1N
- R21 pad 1: ECC_4P -> ECC_3P
- R22 pad 1: ECC_3P -> VDDA
- R22 pad 2: VDDA -> ECC_3P
- R23 pad 1: VDDA -> ECC_4N
- R23 pad 2: ECC_4P -> VDDA
- R24 pad 2: ECC_3P -> ECC_4N
- R25 pad 1: ECC_6P -> Net-(C19-Pad1)
- R25 pad 2: VDDA -> /EEGFrontendElectrode1To4/ELECTRODE_6
- R26 pad 1: ECC_5P -> Net-(C20-Pad1)
- R26 pad 2: VDDA -> /EEGFrontendElectrode1To4/ELECTRODE_3
- R27 pad 1: VDDA -> Net-(C21-Pad1)
- R27 pad 2: ECC_6P -> Net-(C19-Pad1)
- R28 pad 1: VDDA -> Net-(C22-Pad1)
- R28 pad 2: ECC_5P -> Net-(C20-Pad1)
- R29 pad 1: ECC_8P -> ECC_2P
- R3 pad 1: Net-(C7-Pad1) -> Net-(C3-Pad1)
- R3 pad 2: /EEGFrontendPositiveElectrode/ELECTRODE_2 -> /EEGFrontendElectrode1To4/ELECTRODE_7
- R30 pad 1: ECC_7P -> VDDA
- R30 pad 2: VDDA -> ECC_2P
- R31 pad 1: VDDA -> ECC_3N
- R31 pad 2: ECC_8P -> VDDA
- R32 pad 2: ECC_7P -> ECC_3N
- R37 pad 1: Net-(C46-Pad1) -> GNDA
- R37 pad 2: Net-(C45-Pad1) -> Net-(JP20-Pad2)
- R38 pad 1: /EEGAcquisition/V_REF -> GNDA
- R38 pad 2: Net-(C48-Pad1) -> Net-(JP21-Pad2)
- R39 pad 1: /EEGAcquisition/V_REF -> GNDA
- R39 pad 2: Net-(C48-Pad2) -> Net-(JP22-Pad2)
- R4 pad 1: Net-(C2-Pad2) -> Net-(C4-Pad1)
- R4 pad 2: Net-(C7-Pad1) -> Net-(C1-Pad1)
- R40 pad 1: ECC_1N -> Net-(C70-Pad1)
- R40 pad 2: VDDA -> /EEGFrontendElectrode5To8/ELECTRODE_4
- R41 pad 1: ECC_2N -> Net-(C71-Pad1)
- R41 pad 2: VDDA -> /EEGFrontendElectrode5To8/ELECTRODE_1
- R42 pad 1: ECC_3N -> Net-(C72-Pad1)
- R42 pad 2: VDDA -> /EEGFrontendElectrode5To8/ELECTRODE_7
- R43 pad 1: Net-(C75-Pad1) -> Net-(C73-Pad1)
- R43 pad 2: /EEGFrontendNegativeElectrode/ELECTRODE_1 -> Net-(C70-Pad1)
- R44 pad 1: Net-(C66-Pad2) -> Net-(C74-Pad1)
- R44 pad 2: Net-(C75-Pad1) -> Net-(C71-Pad1)
- R45 pad 1: Net-(C77-Pad1) -> Net-(C75-Pad1)
- R45 pad 2: /EEGFrontendNegativeElectrode/ELECTRODE_2 -> Net-(C72-Pad1)
- R46 pad 1: Net-(C73-Pad2) -> ECC_5P
- R46 pad 2: Net-(C77-Pad1) -> VDDA
- R47 pad 1: Net-(C79-Pad1) -> VDDA
- R47 pad 2: /EEGFrontendNegativeElectrode/ELECTRODE_3 -> ECC_5P
- R48 pad 1: Net-(C74-Pad2) -> ECC_6N
- R48 pad 2: Net-(C79-Pad1) -> VDDA
- R49 pad 2: ECC_1N -> ECC_6N
- R5 pad 1: Net-(C9-Pad1) -> Net-(C5-Pad1)
- R5 pad 2: /EEGFrontendPositiveElectrode/ELECTRODE_3 -> Net-(C2-Pad1)
- R50 pad 1: VDDA -> ECC_8P
- R50 pad 2: ECC_2N -> VDDA
- R51 pad 2: ECC_3N -> ECC_8P
- R52 pad 1: ECC_6N -> Net-(C79-Pad1)
- R52 pad 2: VDDA -> /EEGFrontendElectrode5To8/ELECTRODE_2
- R53 pad 1: ECC_4N -> Net-(C80-Pad1)
- R53 pad 2: VDDA -> /EEGFrontendElectrode5To8/ELECTRODE_8
- R54 pad 1: ECC_5N -> Net-(C81-Pad1)
- R54 pad 2: VDDA -> /EEGFrontendElectrode5To8/ELECTRODE_5
- R55 pad 1: Net-(C84-Pad1) -> Net-(C82-Pad1)
- R55 pad 2: /EEGFrontendNegativeElectrode/ELECTRODE_6 -> Net-(C79-Pad1)
- R56 pad 1: Net-(C81-Pad2) -> Net-(C83-Pad1)
- R56 pad 2: Net-(C84-Pad1) -> Net-(C80-Pad1)
- R57 pad 1: Net-(C86-Pad1) -> Net-(C84-Pad1)
- R57 pad 2: /EEGFrontendNegativeElectrode/ELECTRODE_4 -> Net-(C81-Pad1)
- R58 pad 1: Net-(C82-Pad2) -> ECC_5N
- R58 pad 2: Net-(C86-Pad1) -> VDDA
- R59 pad 1: Net-(C88-Pad1) -> VDDA
- R59 pad 2: /EEGFrontendNegativeElectrode/ELECTRODE_5 -> ECC_5N
- R6 pad 1: Net-(C10-Pad1) -> Net-(C6-Pad1)
- R6 pad 2: Net-(C9-Pad1) -> Net-(C3-Pad1)
- R60 pad 1: Net-(C83-Pad2) -> ECC_7P
- R60 pad 2: Net-(C88-Pad1) -> VDDA
- R61 pad 2: ECC_6N -> ECC_7P
- R62 pad 1: VDDA -> ECC_8N
- R62 pad 2: ECC_4N -> VDDA
- R63 pad 2: ECC_5N -> ECC_8N
- R64 pad 1: ECC_8N -> Net-(C88-Pad1)
- R64 pad 2: VDDA -> /EEGFrontendElectrode5To8/ELECTRODE_6
- R65 pad 1: ECC_7N -> Net-(C89-Pad1)
- R65 pad 2: VDDA -> /EEGFrontendElectrode5To8/ELECTRODE_3
- R66 pad 1: Net-(C92-Pad1) -> Net-(C90-Pad1)
- R66 pad 2: /EEGFrontendNegativeElectrode/ELECTRODE_8 -> Net-(C88-Pad1)
- R67 pad 1: Net-(C90-Pad2) -> Net-(C91-Pad1)
- R67 pad 2: Net-(C92-Pad1) -> Net-(C89-Pad1)
- R68 pad 1: Net-(C94-Pad1) -> ECC_6P
- R68 pad 2: /EEGFrontendNegativeElectrode/ELECTRODE_7 -> VDDA
- R69 pad 1: Net-(C91-Pad2) -> VDDA
- R69 pad 2: Net-(C94-Pad1) -> ECC_6P
- R7 pad 1: Net-(C11-Pad1) -> ECC_1P
- R7 pad 2: /EEGFrontendPositiveElectrode/ELECTRODE_4 -> VDDA
- R70 pad 1: VDDA -> ECC_7N
- R70 pad 2: ECC_8N -> VDDA
- R8 pad 1: Net-(C12-Pad1) -> VDDA
- R8 pad 2: Net-(C11-Pad1) -> ECC_1P
- R9 pad 1: Net-(C13-Pad1) -> ECC_2N
- R9 pad 2: /EEGFrontendPositiveElectrode/ELECTRODE_5 -> VDDA
- TP1 pad 1: Net-(TP1-Pad1) -> Net-(JP17-Pad2)
- TP10 pad 1: EEG_CS -> Net-(C60-Pad1)
- TP11 pad 1: EEG_MOSI -> VDDA
- TP2 pad 1: Net-(TP2-Pad1) -> Net-(JP18-Pad2)
- TP3 pad 1: ECC_POWER_SUPPLY -> Net-(C37-Pad1)
- TP4 pad 1: VDDA -> EEG_MISO
- TP5 pad 1: VDDA -> EEG_SCK
- TP6 pad 1: Net-(C71-Pad1) -> EEG_CS
- TP7 pad 1: VDDA -> EEG_MOSI
- TP8 pad 1: EEG_MISO -> ECC_POWER_SUPPLY
- TP9 pad 1: EEG_SCK -> ECC_POWER_SUPPLY
- U1 pad 17: Net-(TP1-Pad1) -> Net-(JP17-Pad2)
- U1 pad 18: Net-(TP2-Pad1) -> Net-(JP18-Pad2)
- U1 pad 24: /EEGAcquisition/V_REF -> Net-(C37-Pad1)
- U1 pad 26: Net-(C33-Pad1) -> Net-(C36-Pad1)
- U1 pad 28: Net-(C25-Pad1) -> Net-(C38-Pad1)
- U1 pad 30: Net-(C34-Pad1) -> Net-(C39-Pad1)
- U1 pad 35: Net-(JP28-Pad2) -> Net-(JP22-Pad2)
- U1 pad 36: Net-(JP27-Pad2) -> Net-(JP21-Pad2)
- U1 pad 37: /EEGAcquisition/CLK -> (no net)
- U1 pad 38: Net-(JP29-Pad2) -> Net-(JP20-Pad2)
- U1 pad 41: GNDA -> Net-(JP19-Pad2)
- U1 pad 52: (no net) -> GNDA
- U1 pad 53: (no net) -> Net-(C41-Pad2)
- U1 pad 54: (no net) -> Net-(C42-Pad1)
- U1 pad 55: Net-(C26-Pad1) -> Net-(C28-Pad1)
- U1 pad 61: (no net) -> /EEGAcquisition/OPAMP_MAYBE
- U1 pad 64: Net-(C31-Pad1) -> Net-(C25-Pad1)
- U2 pad 2: Net-(U2-Pad2) -> /EEGAcquisition/OPAMP_MAYBE
- U2 pad 6: Net-(U2-Pad2) -> /EEGAcquisition/OPAMP_MAYBE
- U4 pad 1: (no net) -> Net-(C50-Pad1)
- U4 pad 2: VDDA -> Net-(C50-Pad1)
- U4 pad 4: VDDA -> (no net)
- U4 pad 5: Net-(C44-Pad1) -> (no net)
- U4 pad 6: Net-(C45-Pad1) -> (no net)
- U5 pad 1: (no net) -> VDDA
- U5 pad 2: Net-(C48-Pad2) -> GNDA
- U5 pad 3: Net-(C46-Pad1) -> (no net)
- U5 pad 4: VDDA -> (no net)
- U5 pad 6: Net-(C48-Pad1) -> (no net)
- U5 pad 7: VDDA -> Net-(JP23-Pad1)
- U5 pad 8: (no net) -> GNDA
- U6 pad 1: VDDA -> Net-(C59-Pad1)
- U6 pad 2: GNDA -> Net-(C57-Pad1)
- U6 pad 4: (no net) -> GNDA
- U6 pad 5: (no net) -> Net-(C58-Pad2)
- U6 pad 7: Net-(JP9-Pad1) -> (no net)
- U6 pad 8: GNDA -> (no net)
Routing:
- added copper zone on F.Cu, net GNDA
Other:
- board outline added: 100 x 100 mm
